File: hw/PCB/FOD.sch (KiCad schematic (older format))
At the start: 9 parts, among them J2 Programmer, U1 SAMD21G, U2 TRH-G2, U3 XA1110, Y1 32.768kHz

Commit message: Added preliminary design of the PC104 board connections.
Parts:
- removed U2: TRH-G2, GPS:TRH-G2, symbol GPS:TRH-G2
- removed U3: XA1110, GPS:XA1110, symbol GPS:XA1110
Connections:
- net labels removed: GPS_INT, GPS_PPS, GPS_RST, GPS_WK
- wire segments 102 -> 87
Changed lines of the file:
@@
 EESchema Schematic File Version 4
-LIBS:Femtosat-cache
+LIBS:FOD-cache
 EELAYER 29 0
 EELAYER END
@@
 	4900 5150 4900 5250
 $Comp
-L GPS:XA1110 U3
-U 1 1 5BD2F968
-P 7600 4700
-F 0 "U3" H 7600 5050 60  0000 C CNN
-F 1 "XA1110" H 7600 4350 60  0000 C CNN
-F 2 "GPS:XA1110" H 7300 4650 60  0001 C CNN
-F 3 "" H 7300 4650 60  0001 C CNN
-	1    7600 4700
-	1    0    0    -1
-$EndComp
-Text Label 6750 4500 0    50   ~ 0
-GPS_INT
-Wire Wire Line
-	7100 4500 6750 4500
-Wire Wire Line
-	6750 4600 7100 4600
-Wire Wire Line
-	7100 4700 6750 4700
-Text Label 6750 4600 0    50   ~ 0
-GND
-Text Label 6750 4700 0    50   ~ 0
-3V3
-Text Label 6750 4800 0    50   ~ 0
-SDA
-Text Label 6750 4900 0    50   ~ 0
-SCL
-Wire Wire Line
-	7100 4800 6750 4800
-Wire Wire Line
-	6750 4900 7100 4900
-Text Label 8450 4500 2    50   ~ 0
-GPS_WK
-Text Label 8450 4600 2    50   ~ 0
-GPS_RST
-Text Label 8450 4700 2    50   ~ 0
-GPS_PPS
-Text Label 8450 4800 2    50   ~ 0
-TX
-Text Label 8450 4900 2    50   ~ 0
-RX
-Wire Wire Line
-	8450 4500 8100 4500
-Wire Wire Line
-	8100 4600 8450 4600
-Wire Wire Line
-	8450 4700 8100 4700
-Wire Wire Line
-	8100 4800 8450 4800
-Wire Wire Line
-	8450 4900 8100 4900
-$Comp
 L Connector:Conn_01x03_Male J2
 U 1 1 5BD799EE
@@
 Wire Wire Line
 	7150 2200 7400 2200
-$Comp
-L GPS:TRH-G2 U2
-U 1 1 5BD83F9A
-P 7550 3350
-F 0 "U2" H 7550 3700 50  0000 C CNN
-F 1 "TRH-G2" H 7800 3050 50  0000 C CNN
-F 2 "GPS:TRH-G2" H 7650 3350 50  0001 C CNN
-F 3 "" H 7650 3350 50  0001 C CNN
-	1    7550 3350
-	1    0    0    -1
-$EndComp
-Wire Wire Line
-	7550 3700 7550 3750
-$Comp
-L power:GND #PWR0111
-U 1 1 5BD888B5
-P 7550 3750
-F 0 "#PWR0111" H 7550 3500 50  0001 C CNN
-F 1 "GND" H 7555 3577 50  0000 C CNN
-F 2 "" H 7550 3750 50  0001 C CNN
-F 3 "" H 7550 3750 50  0001 C CNN
-	1    7550 3750
-	1    0    0    -1
-$EndComp
-Wire Wire Line
-	8050 3450 8200 3450
-Text Label 6700 3150 0    50   ~ 0
-5V0
-Text Label 6700 3250 0    50   ~ 0
-GPS_RST
-Text Label 6700 3450 0    50   ~ 0
-TX
-Text Label 8200 3450 2    50   ~ 0
-RX
-Wire Wire Line
-	6700 3150 7050 3150
-Wire Wire Line
-	6700 3250 7050 3250
-Wire Wire Line
-	6700 3450 7050 3450
 $EndSCHEMATC

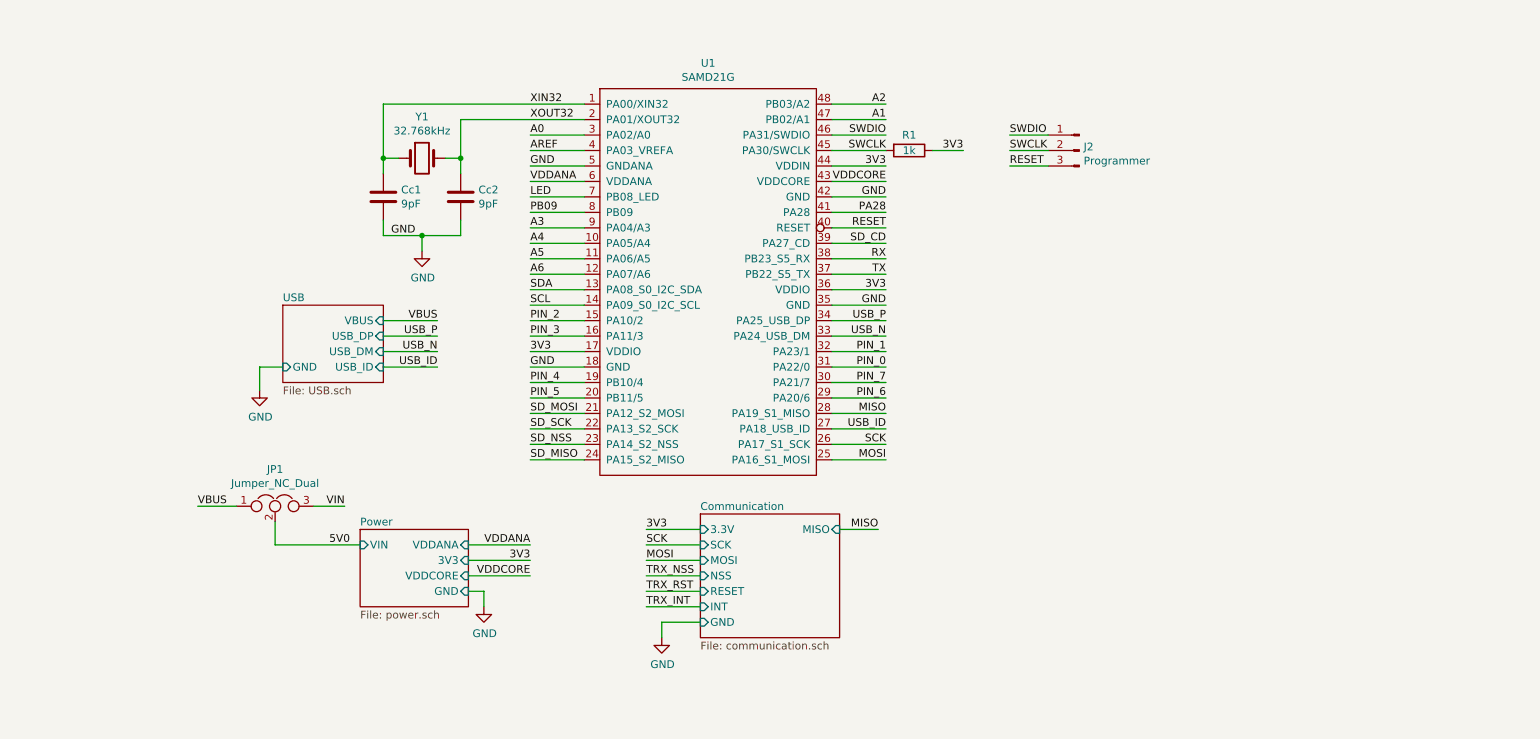
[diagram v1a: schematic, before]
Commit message: Updated PCB's schematic.
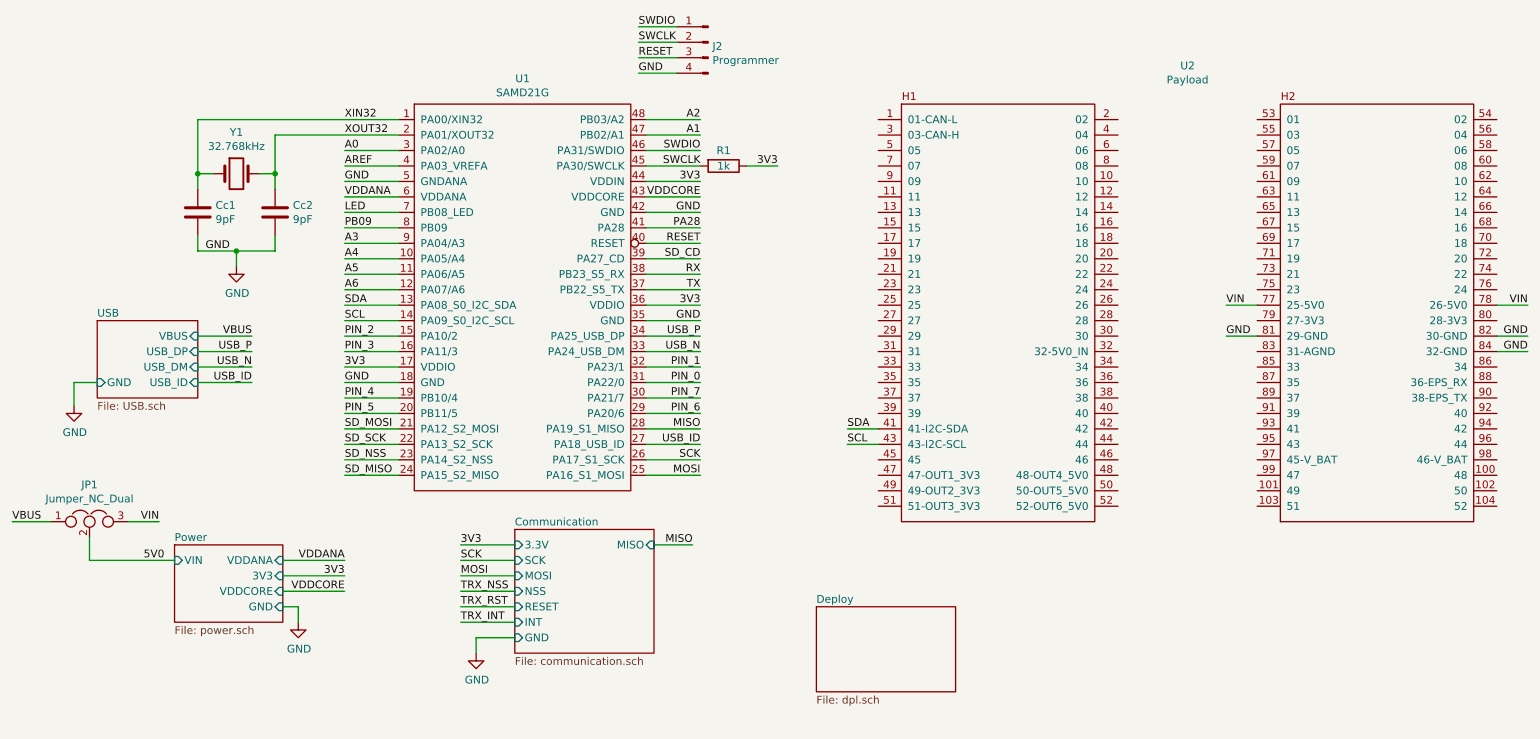
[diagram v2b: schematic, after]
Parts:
- removed J2: Programmer, Connector_PinSocket_2.54mm:PinSocket_1x03_P2.54mm_Vertical, symbol Connector:Conn_01x03_Male
- added J2: Programmer, Connector_PinHeader_2.54mm:PinHeader_1x04_P2.54mm_Vertical, symbol Connector:Conn_01x04_Male
- added U2: Payload, Payload:FOD, symbol Payload:Payload
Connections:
- net GND: now also J2.4 (Pin_4), U2.81 (29-GND), U2.82 (30-GND), U2.84 (32-GND)
- net RESET: now also J2.3 (Pin_3)
- net SCL: now also U2.43 (43-I2C-SCL)
- net SDA: now also U2.41 (41-I2C-SDA)
- net SWCLK: now also J2.2 (Pin_2)
- net SWDIO: now also J2.1 (Pin_1)
- net VIN: now also U2.77 (25-5V0), U2.78 (26-5V0)
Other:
- moved on the sheet: Cc1, Cc2, JP1, R1, U1, Y1

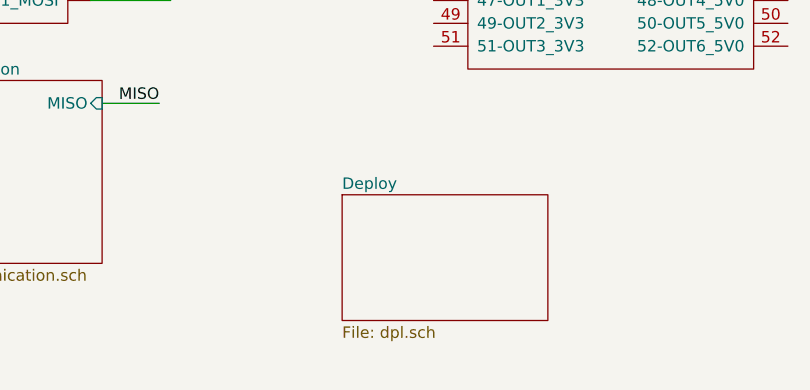
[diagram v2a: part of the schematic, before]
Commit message: Added pin labels for the femto-satellite deploy system.
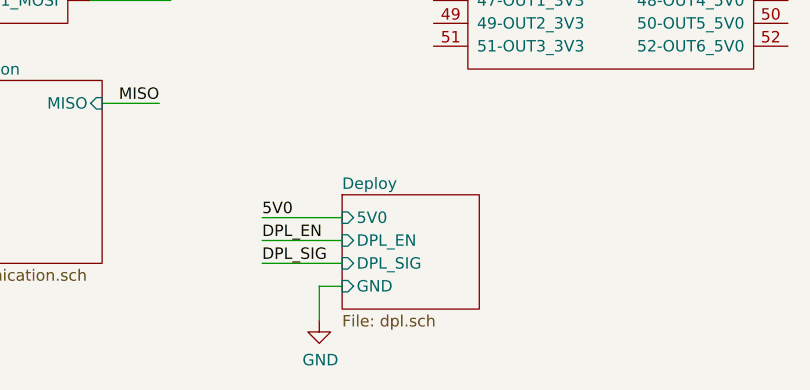
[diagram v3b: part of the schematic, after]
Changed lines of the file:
@@
 GND
 $Sheet
-S 5900 5050 900  550
+S 5900 5050 600  500
 U 5BEF8C81
 F0 "Deploy" 50
 F1 "dpl.sch" 50
+F2 "DPL_EN" I L 5900 5250 50
+F3 "DPL_SIG" I L 5900 5350 50
+F4 "GND" I L 5900 5450 50
+F5 "5V0" I L 5900 5150 50
 $EndSheet
+Text Label 5550 5250 0    50   ~ 0
+DPL_EN
+Text Label 5550 5350 0    50   ~ 0
+DPL_SIG
+Text Label 5550 5150 0    50   ~ 0
+5V0
+Wire Wire Line
+	5900 5150 5550 5150
+Wire Wire Line
+	5550 5250 5900 5250
+Wire Wire Line
+	5900 5350 5550 5350
+$Comp
+L power:GND #PWR?
+U 1 1 5BEB2B09
+P 5800 5600
+F 0 "#PWR?" H 5800 5350 50  0001 C CNN
+F 1 "GND" H 5805 5427 50  0000 C CNN
+F 2 "" H 5800 5600 50  0001 C CNN
+F 3 "" H 5800 5600 50  0001 C CNN
+	1    5800 5600
+	1    0    0    -1
+$EndComp
+Wire Wire Line
+	5900 5450 5800 5450
+Wire Wire Line
+	5800 5450 5800 5600
 $EndSCHEMATC

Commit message: Added the deployment system to the board's footprint.
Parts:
- R1: footprint Resistor_SMD:R_0805_2012Metric_Pad1.15x1.40mm_HandSolder -> Resistor_SMD:R_0603_1608Metric_Pad1.05x0.95mm_HandSolder
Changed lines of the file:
@@
 F 0 "R1" V 5200 2200 50  0000 C CNN
 F 1 "1k" V 5300 2200 50  0000 C CNN
-F 2 "Resistor_SMD:R_0805_2012Metric_Pad1.15x1.40mm_HandSolder" V 5230 2200 50  0001 C CNN
+F 2 "Resistor_SMD:R_0603_1608Metric_Pad1.05x0.95mm_HandSolder" V 5230 2200 50  0001 C CNN
 F 3 "~" H 5300 2200 50  0001 C CNN
 	1    5300 2200

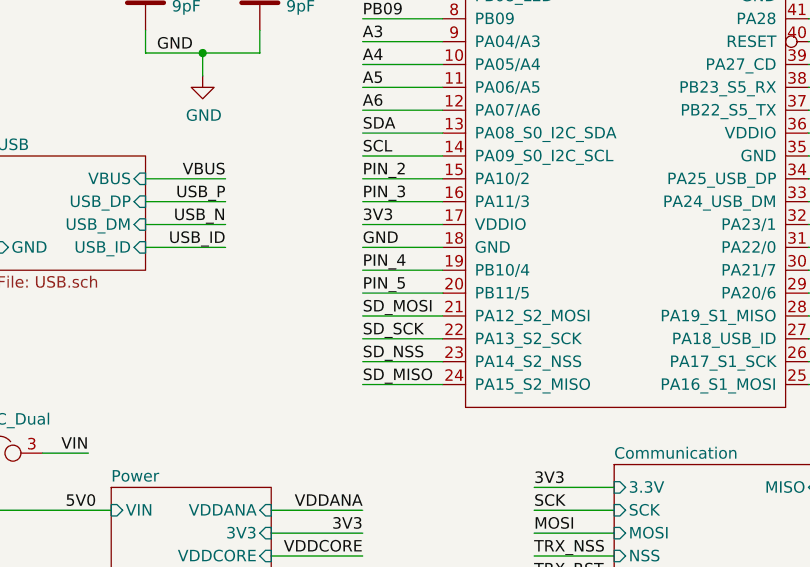
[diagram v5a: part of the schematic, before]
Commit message: Added new connections and 3D models. Most components are now placed in the PCB.
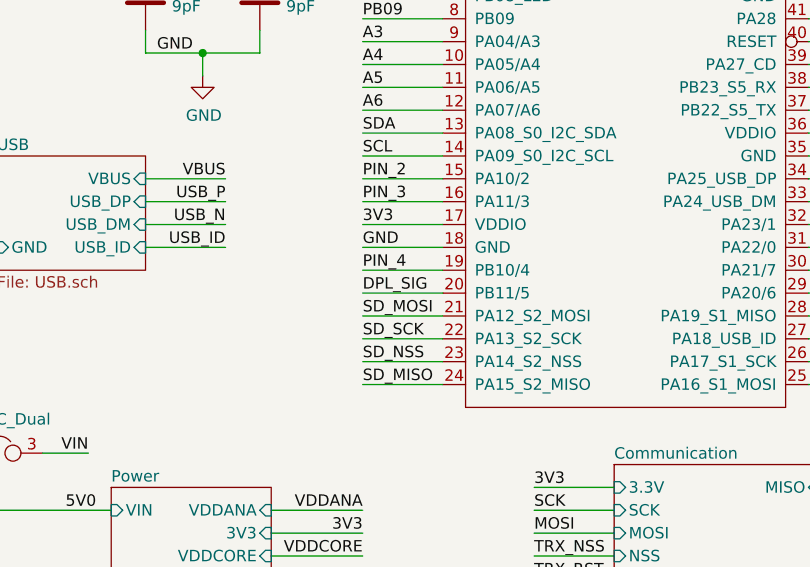
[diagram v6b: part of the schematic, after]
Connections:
- net PIN_5 is gone; now on net DPL_SIG: U1.20 (PB11/5)
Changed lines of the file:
@@
 Text Label 2850 4200 0    50   ~ 0
 SD_MISO
-Text Label 2850 3800 0    50   ~ 0
-PIN_5
 Text Label 2850 3700 0    50   ~ 0
 PIN_4
@@
 Wire Wire Line
 	5800 5450 5800 5600
+Text Label 2850 3800 0    50   ~ 0
+DPL_SIG
 $EndSCHEMATC

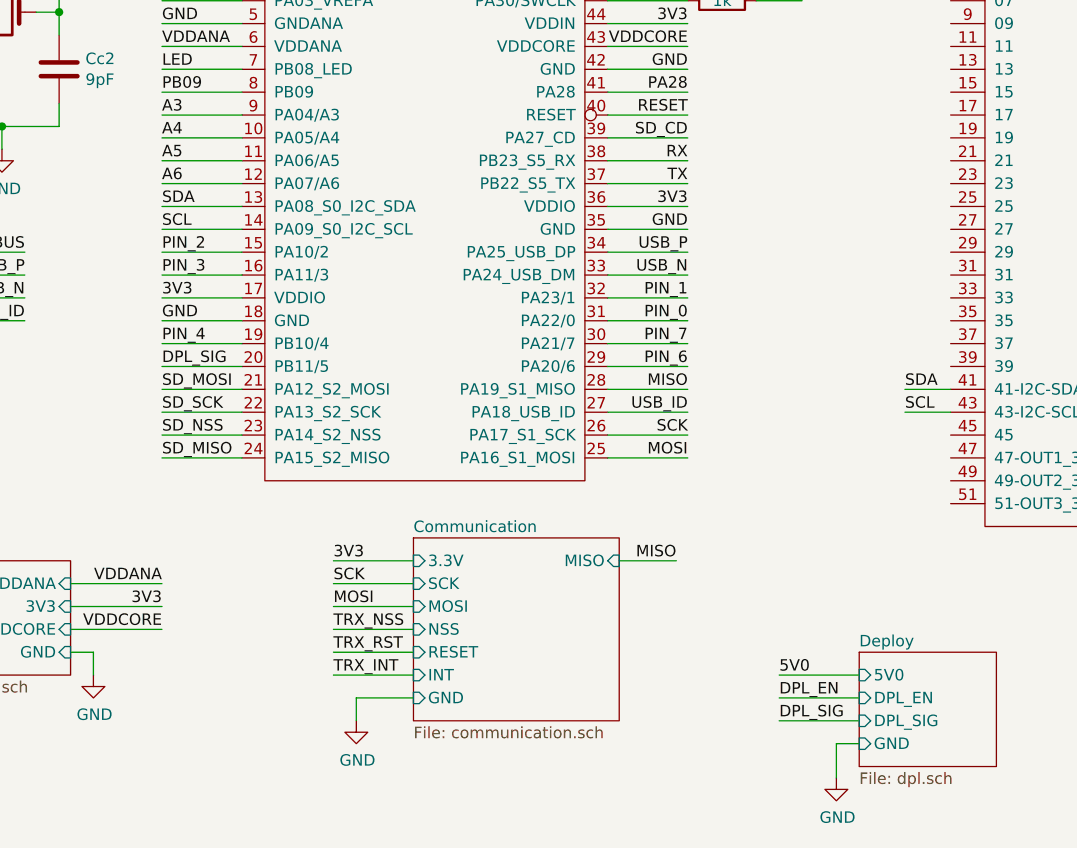
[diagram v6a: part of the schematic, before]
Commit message: Added switch to detect the deplyment status. Routed all connections.
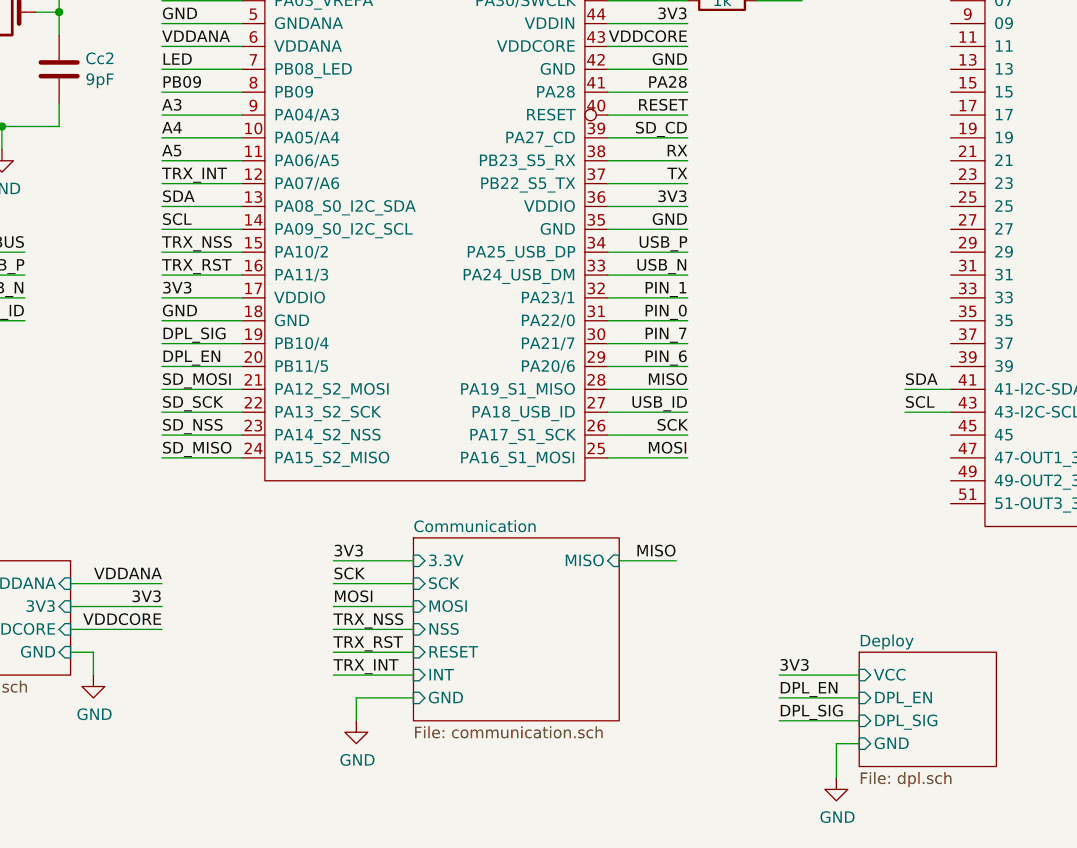
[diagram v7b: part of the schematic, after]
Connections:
- net A6 is gone; now on net TRX_INT: U1.12 (PA07/A6)
- net PIN_2 is gone; now on net TRX_NSS: U1.15 (PA10/2)
- net PIN_3 is gone; now on net TRX_RST: U1.16 (PA11/3)
- net PIN_4 is gone; now on net DPL_SIG: U1.19 (PB10/4)
- net DPL_EN: now also U1.20 (PB11/5)
- net DPL_SIG: no longer U1.20 (PB11/5)
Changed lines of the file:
@@
 Text Label 2850 4200 0    50   ~ 0
 SD_MISO
-Text Label 2850 3700 0    50   ~ 0
-PIN_4
 Text Label 2850 3600 0    50   ~ 0
 GND
 Text Label 2850 3500 0    50   ~ 0
 3V3
-Text Label 2850 3400 0    50   ~ 0
-PIN_3
-Text Label 2850 3300 0    50   ~ 0
-PIN_2
 Text Label 2850 3200 0    50   ~ 0
 SCL
 Text Label 2850 3100 0    50   ~ 0
 SDA
-Text Label 2850 3000 0    50   ~ 0
-A6
 Text Label 2850 2900 0    50   ~ 0
 A5
@@
 F3 "DPL_SIG" I L 5900 5350 50
 F4 "GND" I L 5900 5450 50
-F5 "5V0" I L 5900 5150 50
+F5 "VCC" I L 5900 5150 50
 $EndSheet
 Text Label 5550 5250 0    50   ~ 0
@@
 DPL_SIG
 Text Label 5550 5150 0    50   ~ 0
-5V0
+3V3
 Wire Wire Line
 	5900 5150 5550 5150
@@
 Wire Wire Line
 	5800 5450 5800 5600
+Text Label 2850 3700 0    50   ~ 0
+DPL_SIG
 Text Label 2850 3800 0    50   ~ 0
-DPL_SIG
+DPL_EN
+Text Label 2850 3300 0    50   ~ 0
+TRX_NSS
+Text Label 2850 3400 0    50   ~ 0
+TRX_RST
+Text Label 2850 3000 0    50   ~ 0
+TRX_INT
 $EndSCHEMATC
